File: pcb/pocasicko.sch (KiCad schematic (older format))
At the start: 17 parts, among them J1 SMA, J2 Header_SMD_01x06, J3 FPC24, Q1 Si2312, SW1 SW_Push, SW2 SW_Push, SW3 SW_Push, SW4 SW_Push, SW5 SW_Push, U1 CMWX1ZZABZ-091, U2 BME680

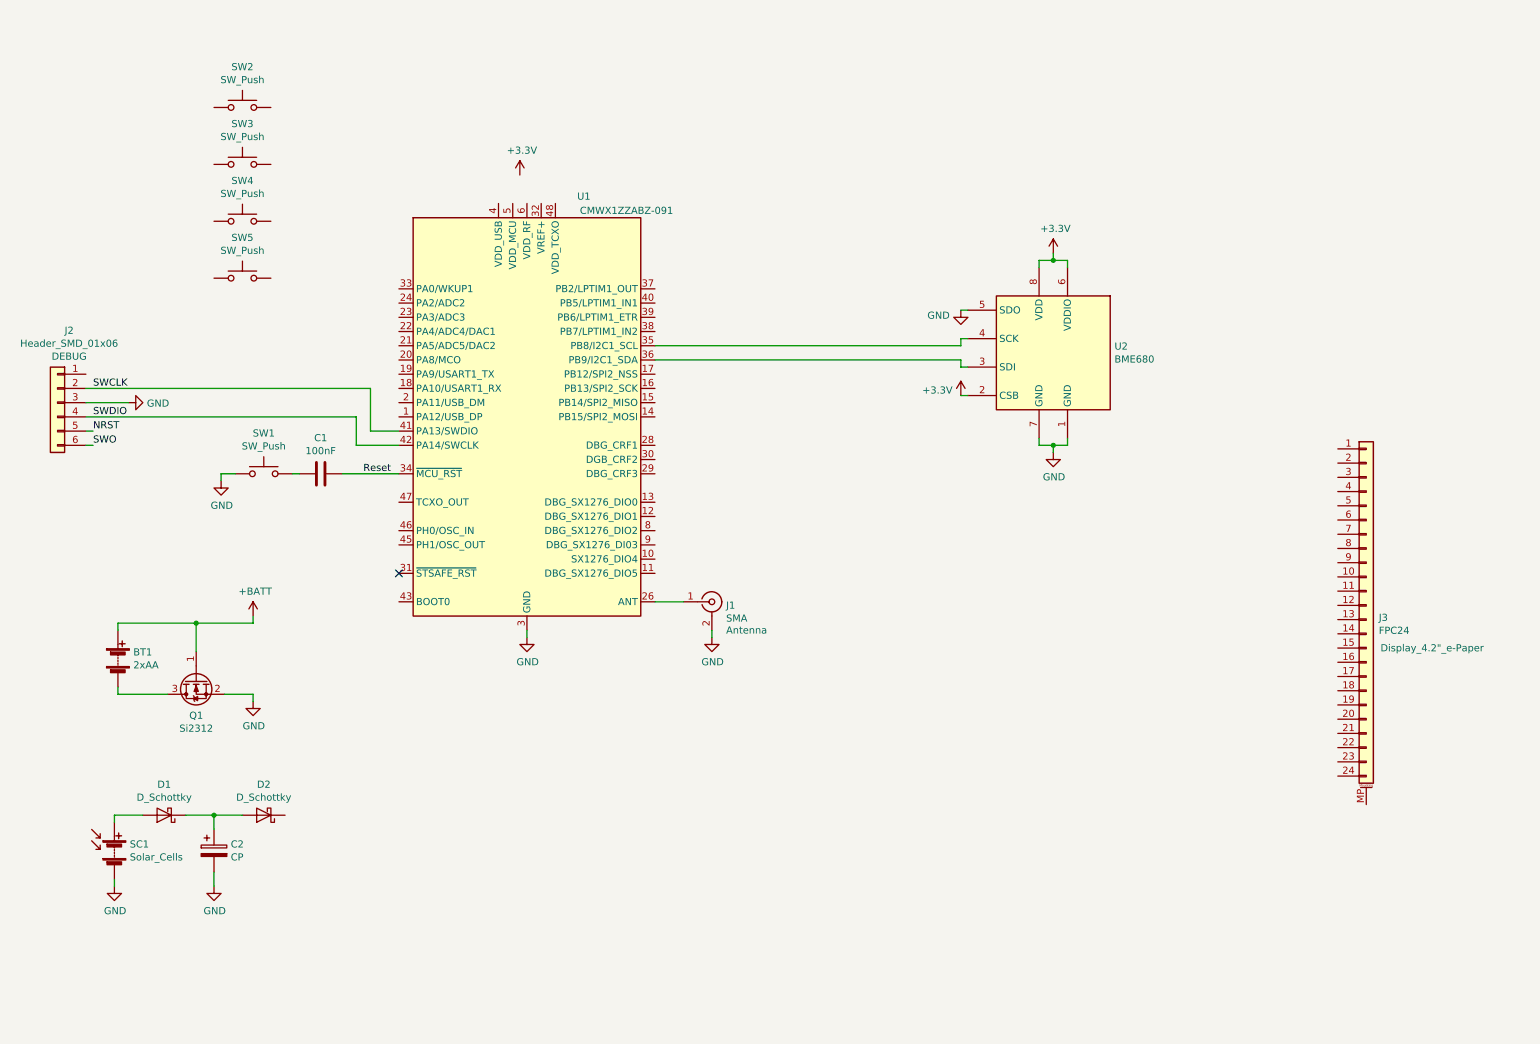
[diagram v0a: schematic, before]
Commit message: Finish schematic and large component placement
All components chosen and placed on the PCB before routing and
schematic probably mostly finished.
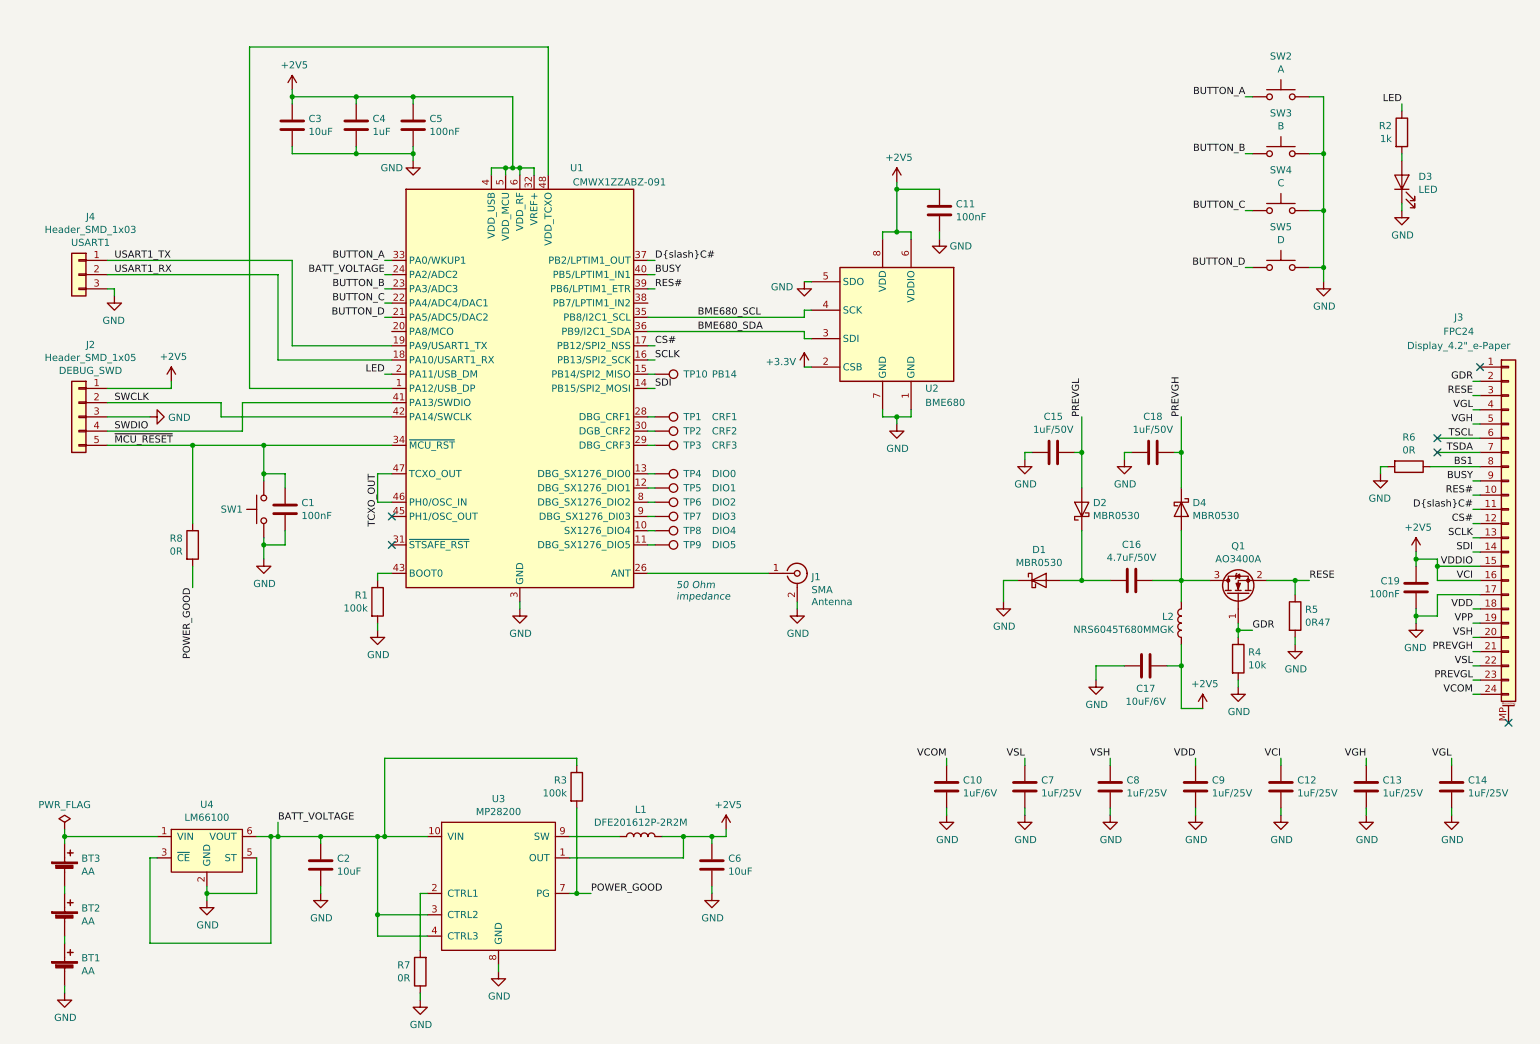
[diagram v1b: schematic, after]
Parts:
- removed BT1: 2xAA, Battery:BatteryHolder_MPD_BC2AAPC_2xAA, symbol Device:Battery
- removed C2: CP, symbol Device:CP
- removed D1, D2: D_Schottky, Diode_SMD:D_SOD-123, symbol Device:D_Schottky
- removed J2: Header_SMD_01x06, Connector_PinHeader_2.54mm:PinHeader_1x06_P2.54mm_Vertical_SMD_Pin1Left, symbol Connector_Generic:Conn_01x06
- removed SC1: Solar_Cells, symbol Device:Solar_Cells
- added BT1, BT2, BT3: AA, Moje:BatteryHolder_Keystone_53_1xAA, symbol Device:Battery_Cell
- added C10: 1uF/6V, Capacitor_SMD:C_0805_2012Metric, symbol Device:C
- added C11, C19, C5: 100nF, Capacitor_SMD:C_0805_2012Metric, symbol Device:C
- added C12, C13, C14, C7, C8, C9: 1uF/25V, Capacitor_SMD:C_0805_2012Metric, symbol Device:C
- added C15, C18: 1uF/50V, Capacitor_SMD:C_1206_3216Metric, symbol Device:C
- added C16: 4.7uF/50V, Capacitor_SMD:C_1206_3216Metric, symbol Device:C
- added C17: 10uF/6V, Capacitor_SMD:C_0805_2012Metric, symbol Device:C
- added C2, C3, C6: 10uF, Capacitor_SMD:C_0805_2012Metric, symbol Device:C
- added C4: 1uF, Capacitor_SMD:C_0805_2012Metric, symbol Device:C
- added D1, D2, D4: MBR0530, Diode_SMD:D_SOD-123, symbol Diode:MBR0530
- added D3: LED, LED_SMD:LED_0805_2012Metric_Castellated, symbol Device:LED
- added J2: Header_SMD_1x05, Connector_PinHeader_2.54mm:PinHeader_1x05_P2.54mm_Vertical_SMD_Pin1Left, symbol Connector_Generic:Conn_01x05
- added J4: Header_SMD_1x03, Connector_PinHeader_2.54mm:PinHeader_1x03_P2.54mm_Vertical_SMD_Pin1Left, symbol Connector_Generic:Conn_01x03
- added L1: DFE201612P-2R2M, Moje:L_0806_2016Metric, symbol Device:L
- added L2: NRS6045T680MMGK, Inductor_SMD:L_Taiyo-Yuden_NR-60xx, symbol Device:L
- added R1, R3: 100k, Resistor_SMD:R_0805_2012Metric, symbol Device:R
- added R2: 1k, Resistor_SMD:R_0805_2012Metric, symbol Device:R
- added R4: 10k, Resistor_SMD:R_0805_2012Metric, symbol Device:R
- added R5: 0R47, Resistor_SMD:R_1206_3216Metric, symbol Device:R
- added R6, R7, R8: 0R, Resistor_SMD:R_0805_2012Metric, symbol Device:R
- added TP1: CRF1, TestPoint:TestPoint_Pad_D1.0mm, symbol Connector:TestPoint
- added TP10: PB14, TestPoint:TestPoint_Pad_D1.0mm, symbol Connector:TestPoint
- added TP2: CRF2, TestPoint:TestPoint_Pad_D1.0mm, symbol Connector:TestPoint
- added TP3: CRF3, TestPoint:TestPoint_Pad_D1.0mm, symbol Connector:TestPoint
- added TP4: DIO0, TestPoint:TestPoint_Pad_D1.0mm, symbol Connector:TestPoint
- added TP5: DIO1, TestPoint:TestPoint_Pad_D1.0mm, symbol Connector:TestPoint
- added TP6: DIO2, TestPoint:TestPoint_Pad_D1.0mm, symbol Connector:TestPoint
- added TP7: DIO3, TestPoint:TestPoint_Pad_D1.0mm, symbol Connector:TestPoint
- added TP8: DIO4, TestPoint:TestPoint_Pad_D1.0mm, symbol Connector:TestPoint
- added TP9: DIO5, TestPoint:TestPoint_Pad_D1.0mm, symbol Connector:TestPoint
- added U3: MP28200, Moje:QFN-12_2x2_Pitch0.4mm, symbol Moje:MP28200
- added U4: LM66100, Package_TO_SOT_SMD:SOT-363_SC-70-6, symbol Moje:LM66100
- J3: footprint Connector_FFC-FPC:Molex_502244-2430_1x24-1MP_P0.5mm_Horizontal -> Moje:Waveshare_EPD_4.2_Amphenol_SFV24R-4STBE1HLF
- Q1: value Si2312 -> AO3400A
- SW1: Comment (none) -> RESET
- SW2: value SW_Push -> A; footprint Button_Switch_SMD:SW_Push_1P1T_NO_6x6mm_H9.5mm -> Button_Switch_SMD:SW_SPST_EVQQ2
- SW3: value SW_Push -> B; footprint Button_Switch_SMD:SW_Push_1P1T_NO_6x6mm_H9.5mm -> Button_Switch_SMD:SW_SPST_EVQQ2
- SW4: value SW_Push -> C; footprint Button_Switch_SMD:SW_Push_1P1T_NO_6x6mm_H9.5mm -> Button_Switch_SMD:SW_SPST_EVQQ2
- SW5: value SW_Push -> D; footprint Button_Switch_SMD:SW_Push_1P1T_NO_6x6mm_H9.5mm -> Button_Switch_SMD:SW_SPST_EVQQ2
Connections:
- net +BATT is gone; now on net GDR: Q1.1 (G)
- net Reset is gone; now on net ~MCU_RESET: C1.1, U1.34 (~MCU_RST)
- net +3V3: no longer U2.6 (VDDIO), U2.8 (VDD)
- net GND: now also C1.2, J3.17 (Pin_17), SW2.2, SW3.2, SW4.2, SW5.2, BT1.2 (-), C10.1, C11.1, C12.1, C13.1, C14.1, C15.2, C17.1, C18.2, C19.1, C2.1, C3.1, C4.1, C5.1, C6.1, C7.1, C8.1, C9.1, D1.1 (K), D3.1 (K), J2.3 (Pin_3), J4.3 (Pin_3), R1.2, R4.2, R5.2, R6.2, R7.1, U3.5 (TP), U3.6 (TP), U3.8 (GND), U4.2 (GND), U4.5 (ST); no longer Q1.2 (S)
- net SWCLK: now also U1.42 (PA14/SWCLK), J2.2 (Pin_2); no longer U1.41 (PA13/SWDIO)
- net SWDIO: now also U1.41 (PA13/SWDIO), J2.4 (Pin_4); no longer U1.42 (PA14/SWCLK)
- net at U1.1 (PA12/USB_DP): now also U1.48 (VDD_TCXO)
- net at U1.10 (SX1276_DIO4): now also TP8.1
- net at U1.11 (DBG_SX1276_DIO5): now also TP9.1
- net at U1.12 (DBG_SX1276_DIO1): now also TP5.1
- net at U1.13 (DBG_SX1276_DIO0): now also TP4.1
- net SDI: now reaches U1.14 (PB15/SPI2_MOSI)
- net SDI: now also J3.14 (Pin_14)
- net at U1.15 (PB14/SPI2_MISO): now also TP10.1
- net SCLK: now reaches U1.16 (PB13/SPI2_SCK)
- net SCLK: now also J3.13 (Pin_13)
- net CS#: now reaches U1.17 (PB12/SPI2_NSS)
- net CS#: now also J3.12 (Pin_12)
- net USART1_RX: now reaches U1.18 (PA10/USART1_RX)
- net USART1_RX: now also J4.2 (Pin_2)
- net USART1_TX: now reaches U1.19 (PA9/USART1_TX)
- net USART1_TX: now also J4.1 (Pin_1)
- net LED: now reaches U1.2 (PA11/USB_DM)
- net LED: now also R2.1
- net BUTTON_D: now reaches U1.21 (PA5/ADC5/DAC2)
- net BUTTON_D: now also SW5.1
- net BUTTON_C: now reaches U1.22 (PA4/ADC4/DAC1)
- net BUTTON_C: now also SW4.1
- net BUTTON_B: now reaches U1.23 (PA3/ADC3)
- net BUTTON_B: now also SW3.1
- net BATT_VOLTAGE: now reaches U1.24 (PA2/ADC2)
- net BATT_VOLTAGE: now also C2.2, R3.1, U3.10 (VIN), U3.3 (CTRL2), U3.4 (CTRL3), U4.3 (~CE), U4.6 (VOUT)
- net at U1.28 (DBG_CRF1): now also TP1.1
- net at U1.29 (DBG_CRF3): now also TP3.1
- net at U1.30 (DGB_CRF2): now also TP2.1
- net +2V5: now reaches U1.32 (VREF+)
- net +2V5: now also J3.15 (Pin_15), J3.16 (Pin_16), U1.4 (VDD_USB), U1.5 (VDD_MCU), U1.6 (VDD_RF), U2.6 (VDDIO), U2.8 (VDD), C11.2, C12.2, C17.2, C19.2, C3.2, C4.2, C5.2, C6.2, J2.1 (Pin_1), L1.2, L2.1, U3.1 (OUT)
- net BUTTON_A: now reaches U1.33 (PA0/WKUP1)
- net BUTTON_A: now also SW2.1
- net BME680_SCL: now reaches U1.35 (PB8/I2C1_SCL), U2.4 (SCK)
- net BME680_SDA: now reaches U1.36 (PB9/I2C1_SDA), U2.3 (SDI)
- net D/C#: now reaches U1.37 (PB2/LPTIM1_OUT)
- net D/C#: now also J3.11 (Pin_11)
- net RES#: now reaches U1.39 (PB6/LPTIM1_ETR)
- net RES#: now also J3.10 (Pin_10)
- net BUSY: now reaches U1.40 (PB5/LPTIM1_IN1)
- net BUSY: now also J3.9 (Pin_9)
- net at U1.43 (BOOT0): now also R1.1
- net TCXO_OUT: now reaches U1.46 (PH0/OSC_IN)
- net TCXO_OUT: now also U1.47 (TCXO_OUT)
- net at U1.8 (DBG_SX1276_DIO2): now also TP6.1
- net at U1.9 (DBG_SX1276_DI03): now also TP7.1
- net at Q1.3 (D): now also C16.1, D4.2 (A), L2.2
- net ~MCU_RESET: now reaches SW1.2
- net ~MCU_RESET: now also J2.5 (Pin_5), R8.1; no longer C1.2
- net VDD: now reaches J3.18 (Pin_18)
- net VDD: now also C9.2
- net VPP: now reaches J3.19 (Pin_19)
- net GDR: now reaches J3.2 (Pin_2)
- net GDR: now also R4.1
- net VSH: now reaches J3.20 (Pin_20)
- net VSH: now also C8.2
- net PREVGH: now reaches J3.21 (Pin_21)
- net PREVGH: now also C18.1, D4.1 (K)
- net VSL: now reaches J3.22 (Pin_22)
- net VSL: now also C7.2
- net PREVGL: now reaches J3.23 (Pin_23)
- net PREVGL: now also C15.1, D2.2 (A)
- net VCOM: now reaches J3.24 (Pin_24)
- net VCOM: now also C10.2
- net RESE: now reaches J3.3 (Pin_3)
- net RESE: now also Q1.2 (S), R5.1
- net VGL: now reaches J3.4 (Pin_4)
- net VGL: now also C14.2
- net VGH: now reaches J3.5 (Pin_5)
- net VGH: now also C13.2
- net TSCL: now reaches J3.6 (Pin_6)
- net TSDA: now reaches J3.7 (Pin_7)
- net BS1: now reaches J3.8 (Pin_8)
- net BS1: now also R6.1
- new net: D3.2 (A), R2.2
- new net: BT2.1 (+), BT3.2 (-)
- new net: BT1.1 (+), BT2.2 (-)
- new net: BT3.1 (+), U4.1 (VIN)
- new net: R7.2, U3.2 (CTRL1)
- new net: L1.1, U3.9 (SW)
- new net: C16.2, D1.2 (A), D2.1 (K)
- new net POWER_GOOD: R3.2, R8.2, U3.7 (PG)
- no-connect marks 1 -> 6
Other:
- note added: "50 Ohm\nimpedance"
- moved on the sheet: C1, J1, J3, SW1, SW2, SW3, SW4, SW5, U1, U2

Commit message: Routing progress
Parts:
- added C20: 1uF, Capacitor_SMD:C_0805_2012Metric, symbol Device:C
- added H1, H2: M3_Hole, MountingHole:MountingHole_3.2mm_M3_DIN965_Pad, symbol Mechanical:MountingHole_Pad
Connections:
- net +3V3 is gone; now on net +2V5: U2.2 (CSB)
- net +2V5: now also C20.2; no longer C12.2
- net GND: now also C20.1
- net VPP: now also C12.2
- no-connect marks 6 -> 8
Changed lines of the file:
@@
-	1    0    0    -1
-$EndComp
-$Comp
-L power:+3.3V #PWR0113
-U 1 1 5DA926E8
-P 6100 3000
-F 0 "#PWR0113" H 6100 2850 50  0001 C CNN
-F 1 "+3.3V" H 6042 3037 50  0000 R CNN
-F 2 "" H 6100 3000 50  0001 C CNN
-F 3 "" H 6100 3000 50  0001 C CNN
-	1    6100 3000
 	1    0    0    -1
 $EndComp
@@
 Wire Wire Line
 	4000 1600 4000 1650
-Wire Wire Line
-	4000 1600 4050 1600
-Wire Wire Line
-	4100 1600 4100 1650
 Connection ~ 4000 1600
-Wire Wire Line
-	4100 1600 4200 1600
-Wire Wire Line
-	4200 1600 4200 1650
-Connection ~ 4100 1600
 $Comp
 L Connector_Generic:Conn_01x05 J2
@@
 	-1   0    0    -1
 $EndComp
-Connection ~ 4050 1600
-Wire Wire Line
-	4050 1600 4100 1600
 $Comp
 L Device:C C3
@@
 Connection ~ 3350 1500
 Wire Wire Line
-	3350 1100 4050 1100
-Wire Wire Line
-	4050 1100 4050 1600
+	3350 1100 4000 1100
+Wire Wire Line
+	4000 1100 4000 1600
 Connection ~ 3350 1100
 Wire Wire Line
@@
 VDD
 Text Label 9450 5750 2    50   ~ 0
-VCI
+VPP
 Text Label 10050 5750 2    50   ~ 0
 VGH
@@
 U 1 1 5D9B77DF
 P 4100 3150
-F 0 "U1" H 4500 4700 50  0000 C CNN
-F 1 "CMWX1ZZABZ-091" H 4800 4600 50  0000 C CNN
+F 0 "U1" H 5000 4500 50  0000 C CNN
+F 1 "CMWX1ZZABZ-091" H 5300 4400 50  0000 C CNN
 F 2 "RF_Module:CMWX1ZZABZ" H 4100 3150 50  0001 C CNN
 F 3 "https://wireless.murata.com/RFM/data/type_abz.pdf" H 6550 1650 50  0001 C CNN
@@
 Wire Wire Line
 	1800 3550 2300 3550
+$Comp
+L Mechanical:MountingHole_Pad H1
+U 1 1 5DB2322A
+P 6750 750
+F 0 "H1" H 6850 799 50  0000 L CNN
+F 1 "M3_Hole" H 6600 950 50  0000 L CNN
+F 2 "MountingHole:MountingHole_3.2mm_M3_DIN965_Pad" H 6750 750 50  0001 C CNN
+F 3 "~" H 6750 750 50  0001 C CNN
+	1    6750 750
+	1    0    0    -1
+$EndComp
+$Comp
+L Mechanical:MountingHole_Pad H2
+U 1 1 5DB28280
+P 7100 750
+F 0 "H2" H 7200 799 50  0000 L CNN
+F 1 "M3_Hole" H 6950 950 50  0000 L CNN
+F 2 "MountingHole:MountingHole_3.2mm_M3_DIN965_Pad" H 7100 750 50  0001 C CNN
+F 3 "~" H 7100 750 50  0001 C CNN
+	1    7100 750
+	1    0    0    -1
+$EndComp
+NoConn ~ 6750 850
+NoConn ~ 7100 850
+$Comp
+L Device:C C20
+U 1 1 5DB46E30
+P 4750 1300
+F 0 "C20" H 4635 1254 50  0000 R CNN
+F 1 "1uF" H 4635 1345 50  0000 R CNN
+F 2 "Capacitor_SMD:C_0805_2012Metric" H 4788 1150 50  0001 C CNN
+F 3 "~" H 4750 1300 50  0001 C CNN
+	1    4750 1300
+	-1   0    0    1
+$EndComp
+$Comp
+L power:+2V5 #PWR0141
+U 1 1 5DB4AB34
+P 4750 1050
+F 0 "#PWR0141" H 4750 900 50  0001 C CNN
+F 1 "+2V5" H 4765 1223 50  0000 C CNN
+F 2 "" H 4750 1050 50  0001 C CNN
+F 3 "" H 4750 1050 50  0001 C CNN
+	1    4750 1050
+	1    0    0    -1
+$EndComp
+Wire Wire Line
+	4750 1150 4750 1100
+$Comp
+L power:GND #PWR0142
+U 1 1 5DB4AFE6
+P 4750 1500
+F 0 "#PWR0142" H 4750 1250 50  0001 C CNN
+F 1 "GND" H 4900 1450 50  0000 C CNN
+F 2 "" H 4750 1500 50  0001 C CNN
+F 3 "" H 4750 1500 50  0001 C CNN
+	1    4750 1500
+	1    0    0    -1
+$EndComp
+Wire Wire Line
+	4750 1500 4750 1450
+Wire Wire Line
+	4750 1100 4200 1100
+Connection ~ 4750 1100
+Wire Wire Line
+	4750 1100 4750 1050
+Wire Wire Line
+	4200 1100 4200 1650
+Wire Wire Line
+	4100 1650 4100 1600
+Wire Wire Line
+	4100 1600 4000 1600
+$Comp
+L power:+2V5 #PWR?
+U 1 1 5DB52717
+P 6100 3000
+F 0 "#PWR?" H 6100 2850 50  0001 C CNN
+F 1 "+2V5" H 6042 3037 50  0000 R CNN
+F 2 "" H 6100 3000 50  0001 C CNN
+F 3 "" H 6100 3000 50  0001 C CNN
+	1    6100 3000
+	1    0    0    -1
+$EndComp
 $EndSCHEMATC

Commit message: Finished routing
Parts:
- added TP11: PA8, TestPoint:TestPoint_Pad_D1.0mm, symbol Connector:TestPoint
- added TP12: PH1, TestPoint:TestPoint_Pad_D1.0mm, symbol Connector:TestPoint
- added TP13: PB7, TestPoint:TestPoint_Pad_D1.0mm, symbol Connector:TestPoint
- SW1: value SW_Push -> RESET
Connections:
- net at U1.20 (PA8/MCO): now also TP11.1
- net at U1.38 (PB7/LPTIM1_IN2): now also TP13.1
- net at U1.45 (PH1/OSC_OUT): now also TP12.1
- net TSCL: no longer names the net of J3.6 (Pin_6)
- net TSDA: no longer names the net of J3.7 (Pin_7)
- no-connect marks 8 -> 7
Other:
- note added: "TSCL"
- note added: "TSDA"
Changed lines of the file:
@@
 P 2300 4000
 F 0 "SW1" V 2300 4148 50  0000 L CNN
-F 1 "SW_Push" H 2300 4200 50  0001 C CNN
+F 1 "RESET" H 2300 4200 50  0001 C CNN
 F 2 "Button_Switch_SMD:SW_Push_1P1T_NO_6x6mm_H9.5mm" H 2300 4200 50  0001 C CNN
 F 3 "~" H 2300 4200 50  0001 C CNN
@@
 Text Label 10800 3400 2    50   ~ 0
 VGH
-Text Label 10800 3500 2    50   ~ 0
-TSCL
-Text Label 10800 3600 2    50   ~ 0
-TSDA
 Text Label 10800 3700 2    50   ~ 0
 BS1
@@
 Wire Wire Line
 	10500 3700 10850 3700
-Wire Wire Line
-	10550 3500 10850 3500
-Wire Wire Line
-	10550 3600 10850 3600
-NoConn ~ 10550 3500
-NoConn ~ 10550 3600
+NoConn ~ 10850 3500
+NoConn ~ 10850 3600
 NoConn ~ 10850 3000
 $Comp
@@
 	1    0    0    -1
 $EndComp
-NoConn ~ 3200 4050
 $Comp
 L Connector_Generic:Conn_01x03 J4
@@
 Wire Wire Line
 	2400 2350 1200 2350
-Text Label 3100 3750 3    50   ~ 0
+Text Label 3150 3750 2    50   ~ 0
 TCXO_OUT
 Text Label 1250 2350 0    50   ~ 0
@@
 	4100 1600 4000 1600
 $Comp
-L power:+2V5 #PWR?
+L power:+2V5 #PWR0113
 U 1 1 5DB52717
 P 6100 3000
-F 0 "#PWR?" H 6100 2850 50  0001 C CNN
+F 0 "#PWR0113" H 6100 2850 50  0001 C CNN
 F 1 "+2V5" H 6042 3037 50  0000 R CNN
 F 2 "" H 6100 3000 50  0001 C CNN
@@
 	1    0    0    -1
 $EndComp
+$Comp
+L Connector:TestPoint TP11
+U 1 1 5DB8A516
+P 3150 2750
+F 0 "TP11" V 3150 2950 50  0000 L CNN
+F 1 "PA8" V 3150 3150 50  0000 L CNN
+F 2 "TestPoint:TestPoint_Pad_D1.0mm" H 3350 2750 50  0001 C CNN
+F 3 "~" H 3350 2750 50  0001 C CNN
+	1    3150 2750
+	0    -1   -1   0
+$EndComp
+Wire Wire Line
+	3150 2750 3200 2750
+$Comp
+L Connector:TestPoint TP13
+U 1 1 5DB8AFB2
+P 5050 2550
+F 0 "TP13" V 5050 2750 50  0000 L CNN
+F 1 "PB7" V 5050 2950 50  0000 L CNN
+F 2 "TestPoint:TestPoint_Pad_D1.0mm" H 5250 2550 50  0001 C CNN
+F 3 "~" H 5250 2550 50  0001 C CNN
+	1    5050 2550
+	0    1    1    0
+$EndComp
+Wire Wire Line
+	5000 2550 5050 2550
+$Comp
+L Connector:TestPoint TP12
+U 1 1 5DB8B425
+P 3150 4050
+F 0 "TP12" V 3200 4200 50  0000 L CNN
+F 1 "PH1" V 3050 4150 50  0000 L CNN
+F 2 "TestPoint:TestPoint_Pad_D1.0mm" H 3350 4050 50  0001 C CNN
+F 3 "~" H 3350 4050 50  0001 C CNN
+	1    3150 4050
+	0    -1   -1   0
+$EndComp
+Wire Wire Line
+	3150 4050 3200 4050
+Text Notes 10600 3500 0    50   ~ 0
+TSCL
+Text Notes 10600 3600 0    50   ~ 0
+TSDA
 $EndSCHEMATC

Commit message: Exchange SMA and add groundplane to the back layer
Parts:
- J1: footprint Connector_Coaxial:SMA_Molex_73251-1153_EdgeMount_Horizontal -> Connector_Coaxial:SMA_Samtec_SMA-J-P-H-ST-EM1_EdgeMount
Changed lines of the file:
@@
 F 0 "J1" H 6150 4425 50  0000 L CNN
 F 1 "SMA" H 6150 4334 50  0000 L CNN
-F 2 "Connector_Coaxial:SMA_Molex_73251-1153_EdgeMount_Horizontal" H 6050 4450 50  0001 C CNN
+F 2 "Connector_Coaxial:SMA_Samtec_SMA-J-P-H-ST-EM1_EdgeMount" H 6050 4450 50  0001 C CNN
 F 3 " ~" H 6050 4450 50  0001 C CNN
 F 4 "Antenna" H 6150 4250 50  0000 L CNN "Comment"
